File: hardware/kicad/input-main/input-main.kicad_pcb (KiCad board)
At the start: 2 copper layers, 132 x 92 mm, 62 parts, among them J1 COMMON_MCU_ADAPTER_2x10, Q1 MMBT3904 RGB OE inverter, SW1 MX 1u soldered prototype, SW10 MX 1u soldered prototype, SW11 MX 1u soldered prototype, SW12 MX 1u soldered prototype, SW13 MX 1u soldered prototype, SW2 MX 1u soldered prototype, SW3 MX 1u soldered prototype, SW4 MX 1u soldered prototype, SW5 MX 1u soldered prototype, SW6 MX 1u soldered prototype, SW7 MX 1u soldered prototype, SW8 MX 1u soldered prototype, SW9 MX 1u soldered prototype, U1 MCP23017-E/SO, U2 AT42QT1010-TSHR, U3 TPS2553DBVR, U4 SN74AHCT1G125DBVR

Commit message: Let every control key communicate agent state without more MCU pins
Constraint: Preserve RGB_DATA and RGB_PWR_EN allocation and the provisional 120 mA aggregate budget
Rejected: Raise the hardware current limit now | Optical, USB-budget, transient, and thermal measurements are not available
Confidence: high
Scope-risk: moderate
Directive: Do not increase RGB current or release Gerbers until the 13-key optical stack and all-white clamp tests pass
Tested: KiCad generator completed; LED1-LED13 chain and C1-C13 asserted; all three schematic ERCs report 0; renders inspected; DRC debt recorded
Not-tested: Physical keycap illumination, full routing, touch-noise immunity, thermal behavior, and first-article current
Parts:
- added C10: 100nF LED local, C_0603_1608Metric, B.Cu at (58.5, 59.0)
- added C11: 100nF LED local, C_0603_1608Metric, B.Cu at (77.5, 59.0)
- added C12: 100nF LED local, C_0603_1608Metric, B.Cu at (96.5, 59.0)
- added C13: 100nF LED local, C_0603_1608Metric, B.Cu at (96.5, 78.0)
- added C7: 100nF LED local, C_0603_1608Metric, B.Cu at (77.5, 40.0)
- added C8: 100nF LED local, C_0603_1608Metric, B.Cu at (96.5, 40.0)
- added C9: 100nF LED local, C_0603_1608Metric, B.Cu at (39.5, 59.0)
- added LED10: SK6812MINI-E, LED_SK6812MINI-E_3.2x2.8mm_P1.5mm_ReverseMount, F.Cu at (47.0, 58.9)
- added LED11: SK6812MINI-E, LED_SK6812MINI-E_3.2x2.8mm_P1.5mm_ReverseMount, F.Cu at (66.0, 58.9)
- added LED12: SK6812MINI-E, LED_SK6812MINI-E_3.2x2.8mm_P1.5mm_ReverseMount, F.Cu at (85.0, 58.9)
- added LED13: SK6812MINI-E, LED_SK6812MINI-E_3.2x2.8mm_P1.5mm_ReverseMount, F.Cu at (85.0, 77.9)
- added LED7: SK6812MINI-E, LED_SK6812MINI-E_3.2x2.8mm_P1.5mm_ReverseMount, F.Cu at (66.0, 39.9)
- added LED8: SK6812MINI-E, LED_SK6812MINI-E_3.2x2.8mm_P1.5mm_ReverseMount, F.Cu at (85.0, 39.9)
- added LED9: SK6812MINI-E, LED_SK6812MINI-E_3.2x2.8mm_P1.5mm_ReverseMount, F.Cu at (28.0, 58.9)
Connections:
- LED6 pad 2: (no net) -> RGB_LINK6

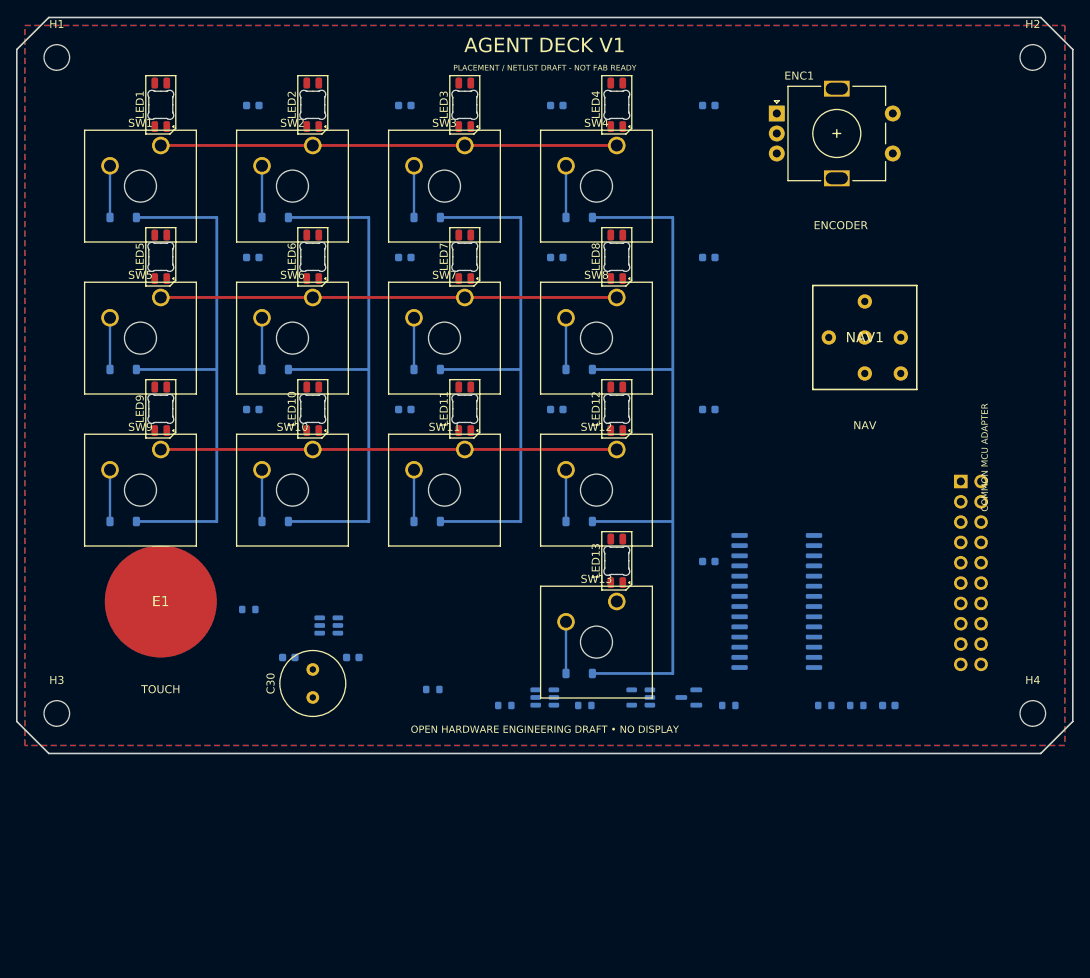
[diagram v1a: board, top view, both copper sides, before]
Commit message: Make the physical control surface serviceable and printable
Constraint: Preserve an independent public-exterior reference without asserting unpublished OpenAI Micro internals.
Rejected: Soldered switches, a square navigation cap, a tall radial bulk capacitor, and the isolated lower-right K13 placement.
Confidence: high
Scope-risk: broad
Directive: Keep this revision out of fabrication until socket, navigation, touch, USB, battery, and first-article fit gates pass.
Tested: KiCad 10.0.4 ERC on all projects; DRC with no short, copper-clearance, hole-clearance, or crossing findings; 13-key/13-LED geometry assertions; Blender 5.1.2 manifold STL generation and visual render review.
Not-tested: Physical switch/socket/joystick samples, printed fit, touch sensitivity, USB cable access, battery fit, antenna performance, or assembled electrical operation.
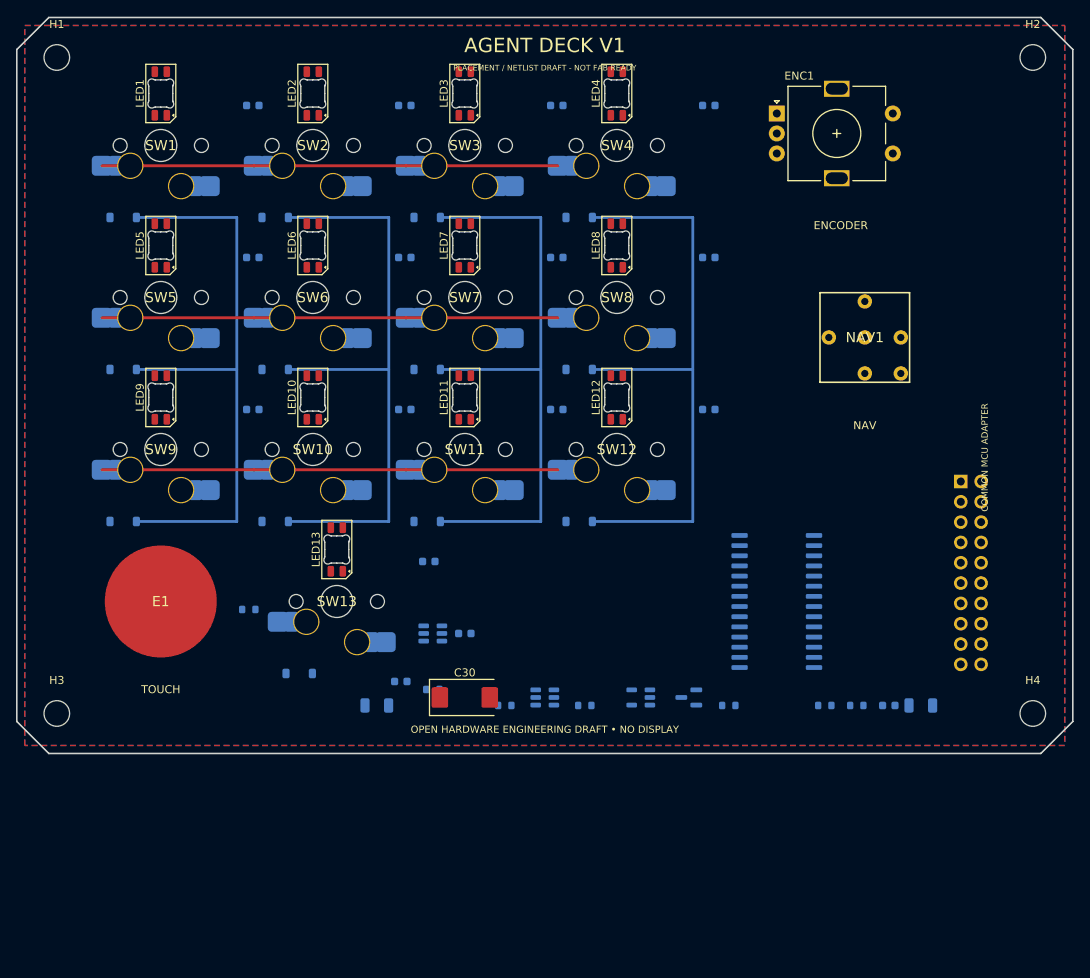
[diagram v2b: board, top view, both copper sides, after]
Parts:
- added C31: 10uF 10V X7R LED rail, C_1206_3216Metric, B.Cu at (55.0, 96.0)
- added C32: 10uF 10V X7R 3V3 rail, C_1206_3216Metric, B.Cu at (123.0, 96.0)
- C30: value 470uF 10V RGB bulk -> 150uF 10V low-profile polymer candidate; footprint C_Radial_D8.0mm_H11.5mm_P3.50mm -> CP_EIA-7343-31_Kemet-D
- NAV1: value SKRHABE010 candidate -> RKJXM1015004 low-profile stick candidate / land pattern provisional; footprint AgentDeck:Nav5_SKRHABE010_PROVISIONAL -> AgentDeck:Nav_RKJXM1015004_ELECTRICAL_PLACEHOLDER
- SW1, SW10, SW11, SW12, SW13, SW2, SW3, SW4, SW5, SW6, SW7, SW8, SW9: value MX 1u soldered prototype -> MX 1u hot-swap / CPG151101S11-16; footprint SW_Cherry_MX_1.00u_Plate -> AgentDeck:MX_1u_Kailh_CPG151101S11-16_Hotswap
- moved LED13 35.0 mm to (50.0, 76.5)
- moved C13 35.0 mm to (61.5, 78.0)
- moved D13 35.0 mm to (45.3, 92.0)
- moved SW13 35.0 mm to (50.0, 83.0)
- moved C30 19.0 mm to (66.0, 95.0), turned to 0 degrees
- moved C20 14.3 mm to (58.0, 93.0)
- moved C21 14.3 mm to (66.0, 87.0)
- moved U2 13.0 mm to (62.0, 87.0)
- moved LED1 1.42 mm to (28.0, 19.5)
- moved LED10 1.42 mm to (47.0, 57.5)
- moved LED11 1.42 mm to (66.0, 57.5)
- moved LED12 1.42 mm to (85.0, 57.5)
- moved LED2 1.42 mm to (47.0, 19.5)
- moved LED3 1.42 mm to (66.0, 19.5)
- moved LED4 1.42 mm to (85.0, 19.5)
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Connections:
- D13 pad 2: COL3 -> COL1
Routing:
- net COL3: track 97.2 -> 75.6 mm
- net COL2: track 68.1 -> 75.6 mm
- net COL1: track 68.1 -> 75.6 mm
- net COL0: track 68.2 -> 75.7 mm
- net K8_D: track 6.46 -> 0.00 mm
- net K7_D: track 6.46 -> 0.00 mm
- net K6_D: track 6.46 -> 0.00 mm
- net K5_D: track 6.46 -> 0.00 mm
- net K4_D: track 6.46 -> 0.00 mm
- net K3_D: track 6.46 -> 0.00 mm
- net K2_D: track 6.46 -> 0.00 mm
- net K1_D: track 6.46 -> 0.00 mm
- net K9_D: track 6.46 -> 0.00 mm
- net K13_D: track 6.46 -> 0.00 mm
- net K12_D: track 6.46 -> 0.00 mm
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
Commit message: Make the controller read as a compact square instrument
Constraint: Preserve standard MX pitch and independent engineering dimensions while following only the public square product language.
Rejected: A square cosmetic shell around the rectangular PCB and uniform scaling that would distort 19 mm switch pitch.
Confidence: high
Scope-risk: broad
Directive: Treat 118 mm as a prototype datum, not an inferred Codex Micro dimension; keep fabrication blocked until component and first-article gates pass.
Tested: KiCad 10.0.4 ERC on all projects; DRC with no short, copper-clearance, hole-clearance, or crossing findings; 118 mm PCB endpoint assertions; 13-key/13-LED coordinate assertions; Blender 5.1.2 square STL generation with zero non-manifold edges.
Not-tested: Physical print, socket and navigation samples, touch performance, USB service opening, battery fit, antenna performance, or assembled electronics.
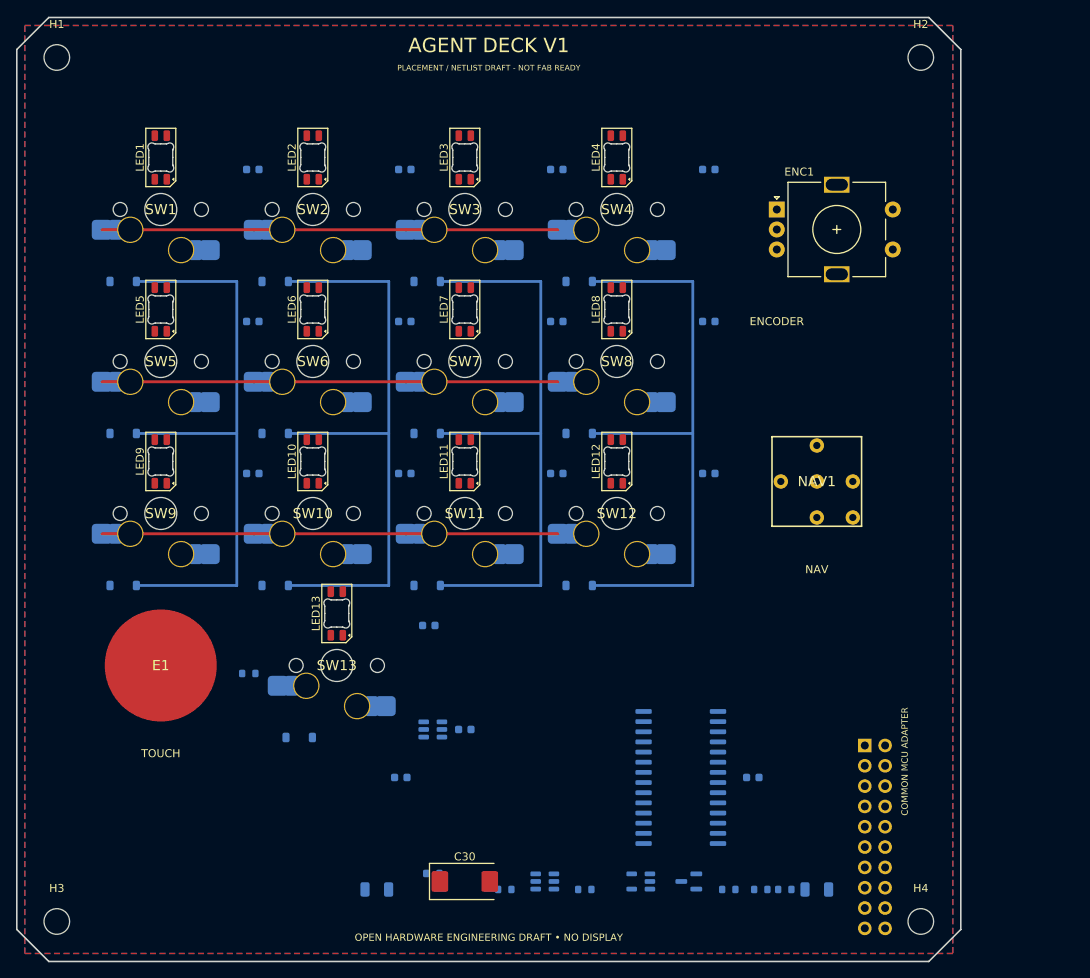
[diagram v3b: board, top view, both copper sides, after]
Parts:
- moved J1 35.1 mm to (116.0, 101.0)
- moved H4 29.5 mm to (123.0, 123.0)
- moved C32 26.4 mm to (110.0, 119.0)
- moved H3 26.0 mm to (15.0, 123.0)
- moved U1 25.1 mm to (93.0, 105.0)
- moved R7 24.7 mm to (106.0, 119.0)
- moved R6 24.4 mm to (103.0, 119.0)
- moved C30 23.0 mm to (66.0, 118.0)
- moved C31 23.0 mm to (55.0, 119.0)
- moved Q1 23.0 mm to (94.0, 118.0)
- moved R2 23.0 mm to (81.0, 119.0)
- moved R3 23.0 mm to (71.0, 119.0)
- moved R4 23.0 mm to (99.0, 119.0)
- moved R5 23.0 mm to (62.0, 117.0)
- moved U3 23.0 mm to (76.0, 118.0)
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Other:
- board size 132 x 92 mm -> 118 x 118 mm

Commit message: Align the physical controls with the observable Codex layout
The square controller now uses twelve hot-swap MX keys so the upper-right position belongs to the navigation control, while K11 remains a wide host-side push-to-talk control.

Constraint: Preserve independent circuitry and avoid claims about unpublished Codex Micro internals

Rejected: Keep a thirteenth MX key in the top row | it displaced the joystick from the observable layout

Confidence: high

Scope-risk: moderate

Directive: Add K11 stabilizer geometry only from the selected part drawing before fabrication

Tested: KiCad ERC on three projects; KiCad DRC and renders on three boards; Blender manifold checks and top-view visual inspection; BOM/JSON parsing; git diff check

Not-tested: Physical fit, touch sensitivity, stabilizer samples, and intentionally open release routing
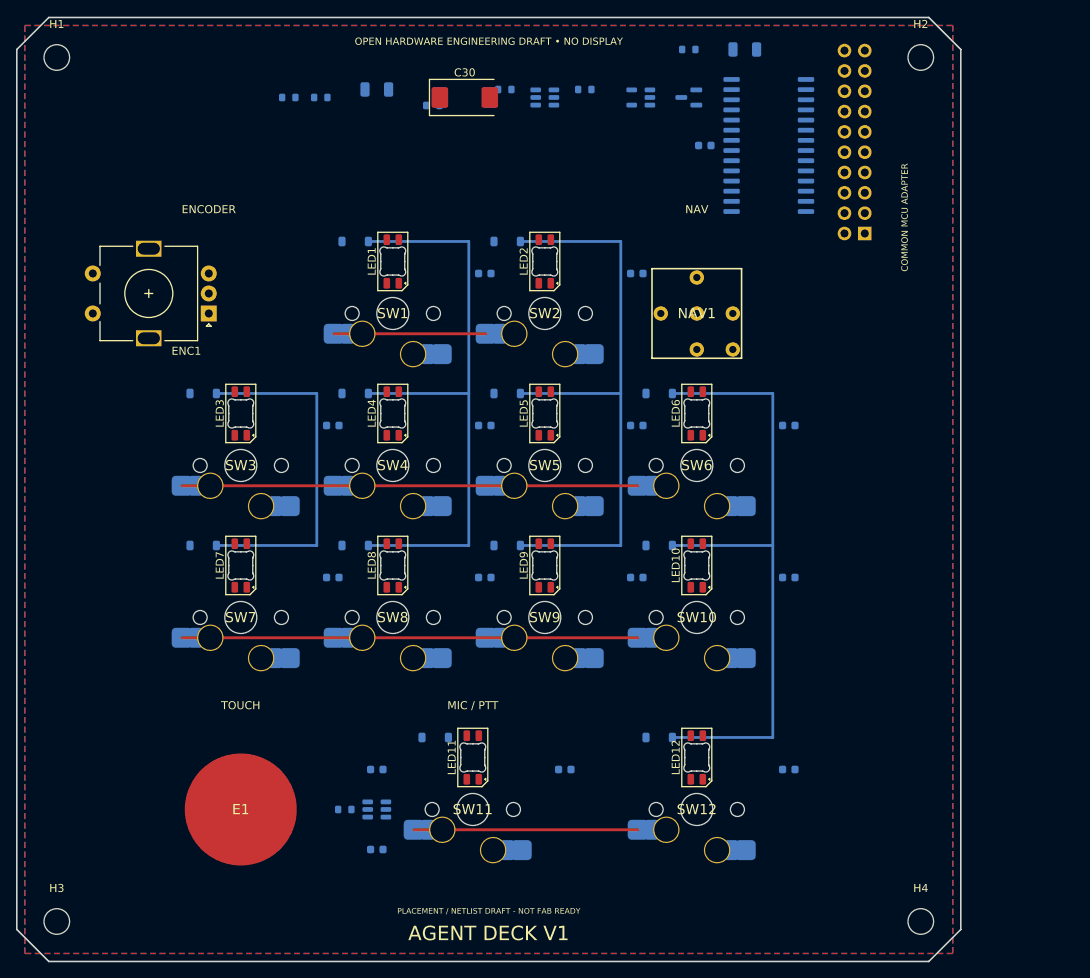
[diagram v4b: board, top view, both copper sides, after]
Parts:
- removed C13: 100nF LED local, C_0603_1608Metric
- removed D13: 1N4148W, D_SOD-123
- removed LED13: SK6812MINI-E, LED_SK6812MINI-E_3.2x2.8mm_P1.5mm_ReverseMount
- removed SW13: MX 1u hot-swap / CPG151101S11-16, AgentDeck:MX_1u_Kailh_CPG151101S11-16_Hotswap
- SW11: value MX 1u hot-swap / CPG151101S11-16 -> MX 2u PTT hot-swap / stabilizer TBD / CPG151101S11-16
- moved R6 115.2 mm to (44.0, 20.0)
- moved R7 114.7 mm to (48.0, 20.0)
- moved C32 105.4 mm to (101.0, 14.0)
- moved R4 105.1 mm to (94.0, 14.0)
- moved C31 100.0 mm to (55.0, 19.0)
- moved R2 100.0 mm to (81.0, 19.0)
- moved R3 100.0 mm to (71.0, 19.0)
- moved C30 98.0 mm to (66.0, 20.0)
- moved Q1 98.0 mm to (94.0, 20.0)
- moved U3 98.0 mm to (76.0, 20.0)
- moved U4 98.0 mm to (88.0, 20.0)
- moved R5 96.0 mm to (62.0, 21.0)
- moved U1 79.8 mm to (104.0, 26.0)
- moved C22 79.2 mm to (96.0, 26.0)
- moved ENC1 72.2 mm to (34.0, 47.0), turned to 180 degrees
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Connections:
- D1 pad 2: COL0 -> COL1
- D10 pad 2: COL1 -> COL3
- D11 pad 2: COL2 -> COL1
- D2 pad 2: COL1 -> COL2
- D3 pad 2: COL2 -> COL0
- D4 pad 2: COL3 -> COL1
- D5 pad 2: COL0 -> COL2
- D6 pad 2: COL1 -> COL3
- D7 pad 2: COL2 -> COL0
- D8 pad 2: COL3 -> COL1
- D9 pad 2: COL0 -> COL2
- LED12 pad 2: RGB_LINK12 -> (no net)
- SW11 pad 1: ROW2 -> ROW3
- SW12 pad 1: ROW2 -> ROW3
- SW3 pad 1: ROW0 -> ROW1
- SW4 pad 1: ROW0 -> ROW1
- SW7 pad 1: ROW1 -> ROW2
- SW8 pad 1: ROW1 -> ROW2
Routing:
- net ROW0: track 57.0 -> 19.0 mm
- net COL0: track 75.7 -> 44.1 mm
- net ROW3: track 0.00 -> 28.0 mm
- net COL3: track 75.6 -> 80.6 mm
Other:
- board text added: "MIC / PTT"

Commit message: Make the key surface read as one coherent status grid
The blank black-smoke keycaps now share one material and a 19 mm lattice, while K11 keeps PTT semantics without permanent artwork.

Constraint: Preserve the 12-key public-facing control map and independent protocol semantics

Rejected: Keep the microphone glyph or colored accents | both broke the uniform configurable key surface

Confidence: high

Scope-risk: moderate

Directive: Qualify actual translucent keycap material and K11 stabilizer from physical samples before fabrication

Tested: Blender manifold generation and top/assembled visual inspection; 1.8 mm gap calculation; KiCad ERC on all projects; main/adapter DRC; KiCad renders; git diff check

Not-tested: Physical keycap optical transmission, RGB diffusion, stabilizer fit, touch sensitivity, intentionally open release routing
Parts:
- moved C11 5.02 mm to (78.0, 99.0)
- moved D11 5.02 mm to (61.8, 95.0)
- moved LED11 5.02 mm to (66.5, 97.5)
- moved SW11 5.02 mm to (66.5, 104.0)
- moved C12 5.00 mm to (106.5, 99.0)
- moved C20 5.00 mm to (55.0, 99.0)
- moved C21 5.00 mm to (55.0, 109.0)
- moved D12 5.00 mm to (90.3, 95.0)
- moved E1 5.00 mm to (38.0, 104.0)
- moved LED12 5.00 mm to (95.0, 97.5)
- moved R1 5.00 mm to (51.0, 104.0)
- moved SW12 5.00 mm to (95.0, 104.0)
- moved U2 5.00 mm to (55.0, 104.0)
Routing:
- net COL3: track 80.6 -> 75.6 mm
- net ROW3: track 28.0 -> 28.5 mm
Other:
- board text added: "PTT"
- board text removed: "MIC / PTT"
